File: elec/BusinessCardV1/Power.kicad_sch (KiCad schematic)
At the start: 0 parts

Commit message: Added BMA400
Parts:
- added U1: *, BMA400:XDCR_BMA400, symbol BMA400:BMA400
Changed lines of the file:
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@@
 	(generator_version "9.0")
 	(paper "A4")
+	(symbol
+		(lib_id "BMA400:BMA400")
+		(at 72.39 64.77 0)
+		(unit 1)
+		(exclude_from_sim no)
+		(in_bom yes)
+		(on_board yes)
+		(dnp no)
+		(fields_autoplaced yes)
+		(property "Reference" "U1"
+			(at 72.39 43.18 0)
+			(effects
+				(font
+					(size 1.8288 1.8288)
+				)
+			)
+		)
+		(property "Value" "*"
+			(at 72.39 46.99 0)
+			(effects
+				(font
+					(size 1.8288 1.8288)
+				)
+			)
+		)
+		(property "Footprint" "BMA400:XDCR_BMA400"
+			(at 72.39 64.77 0)
+			(effects
+				(font
+					(size 1.27 1.27)
+				)
+				(hide yes)
+			)
+		)
+		(property "Datasheet" ""
+			(at 72.39 64.77 0)
+			(effects
+				(font
+					(size 1.27 1.27)
+				)
+				(hide yes)
+			)
+		)
+		(property "Description" "Accelerometer X, Y, Z Axis ±2g, 4g, 8g, 16g - 12-LGA (2x2)"
+			(at 72.39 64.77 0)
+			(effects
+				(font
+					(size 1.27 1.27)
+				)
+				(hide yes)
+			)
+		)
+		(property "SnapEDA_Link" "https://www.snapeda.com/parts/BMA400/Bosch+Sensortec/view-part/?ref=snap"
+			(at 72.39 64.77 0)
+			(effects
+				(font
+					(size 1.8288 1.8288)
+				)
+				(justify left)
+				(hide yes)
+			)
+		)
+		(property "Package" "LGA-12 Bosch Tools"
+			(at 72.39 64.77 0)
+			(effects
+				(font
+					(size 1.8288 1.8288)
+				)
+				(justify left)
+				(hide yes)
+			)
+		)
+		(property "ALTIUM_VALUE" "*"
+			(at 72.39 64.77 0)
+			(effects
+				(font
+					(size 1.8288 1.8288)
+				)
+				(justify left)
+				(hide yes)
+			)
+		)
+		(property "MF" "Bosch Sensortec"
+			(at 72.39 64.77 0)
+			(effects
+				(font
+					(size 1.8288 1.8288)
+				)
+				(justify left)
+				(hide yes)
+			)
+		)
+		(property "MP" "BMA400"
+			(at 72.39 64.77 0)
+			(effects
+				(font
+					(size 1.8288 1.8288)
+				)
+				(justify left)
+				(hide yes)
+			)
+		)
+		(property "Check_prices" "https://www.snapeda.com/parts/BMA400/Bosch+Sensortec/view-part/?ref=eda"
+			(at 72.39 64.77 0)
+			(effects
+				(font
+					(size 1.8288 1.8288)
+				)
+				(justify left)
+				(hide yes)
+			)
+		)
+		(pin "7"
+		)
+		(pin "3"
+		)
+		(pin "10"
+		)
+		(pin "12"
+		)
+		(pin "2"
+		)
+		(pin "1"
+		)
+		(pin "5"
+		)
+		(pin "9"
+		)
+		(pin "6"
+		)
+		(pin "8"
+		)
+		(instances
+			(project ""
+				(path "/28a1e4b0-497b-455a-8c80-759850e7b173/9de3a60e-6635-4d18-85fa-31055f93e53d"
+					(reference "U1")
+					(unit 1)
+				)
+			)
+		)
+	)
 )

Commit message: Big Ballz
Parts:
- added D1: QBLP595-R, FP-QBLP595-R-MFG, symbol QBLP595:QTB-LED-0002

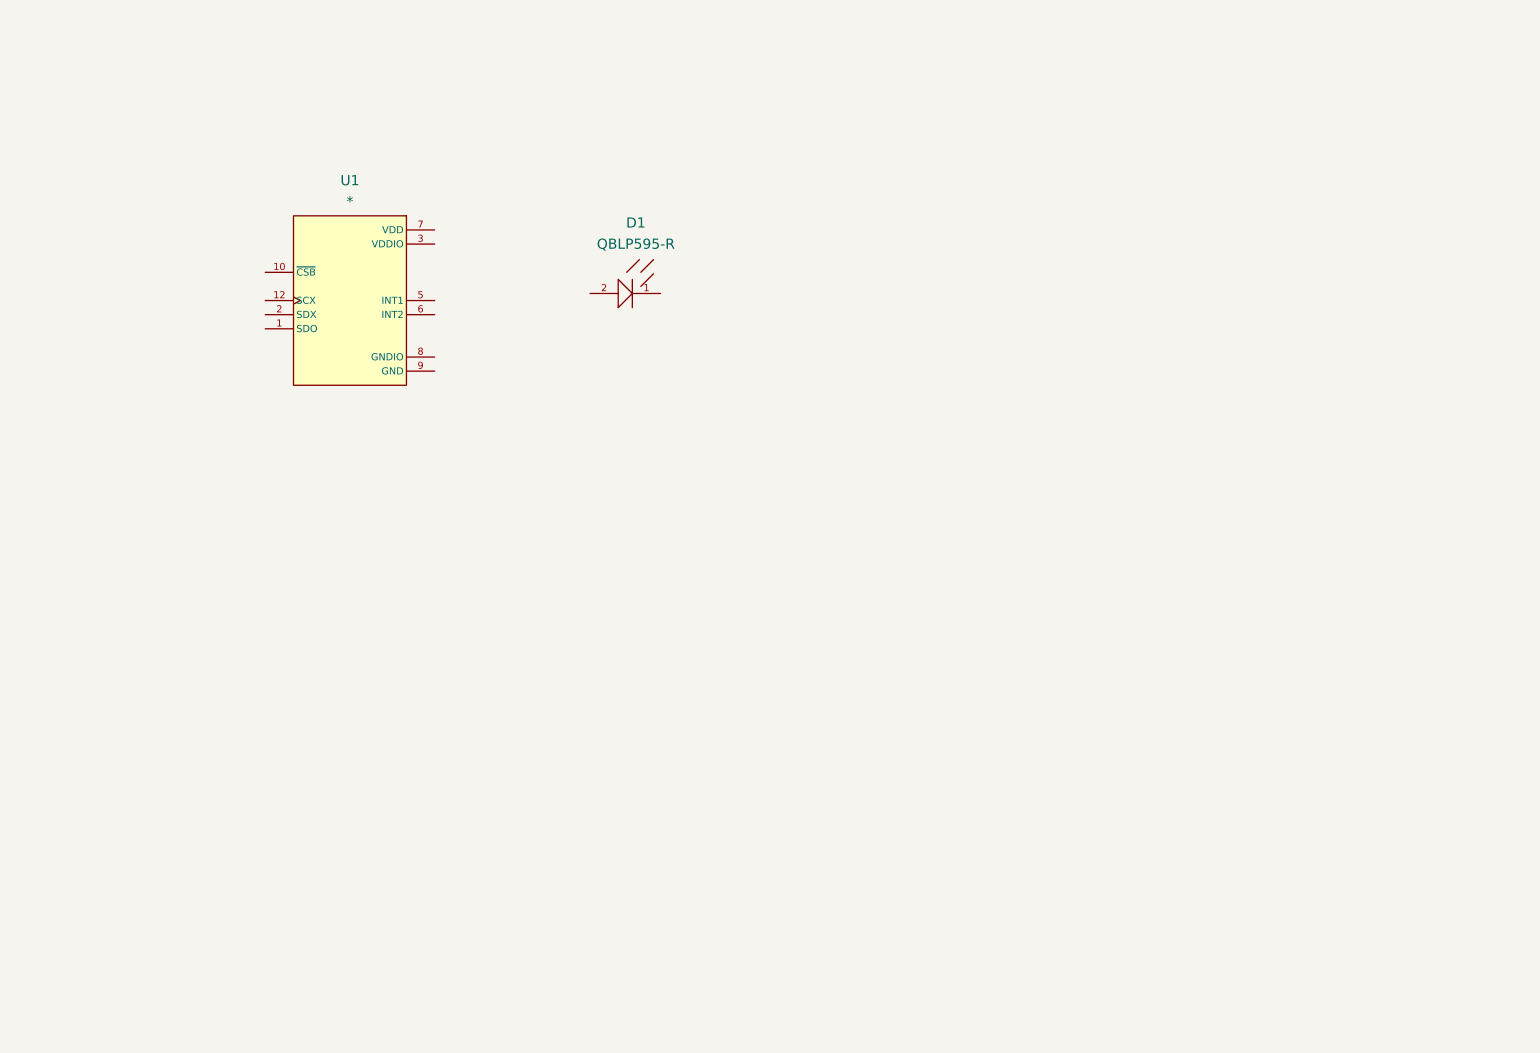
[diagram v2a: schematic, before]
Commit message: Started the power management
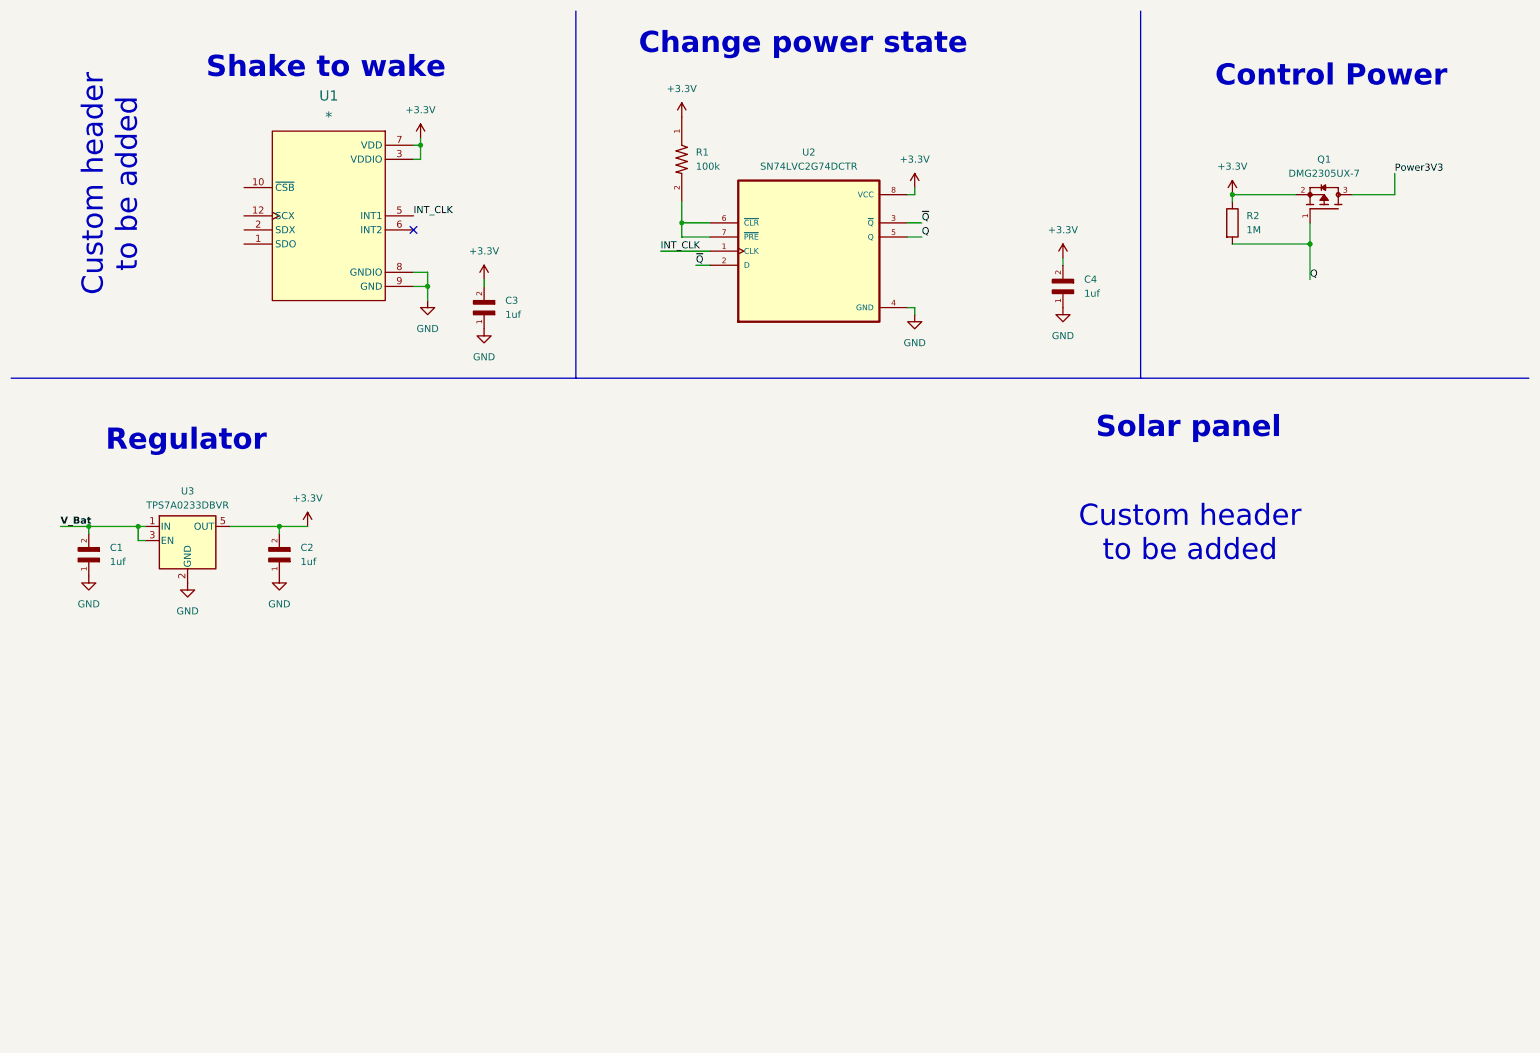
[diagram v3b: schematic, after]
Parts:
- removed D1: QBLP595-R, FP-QBLP595-R-MFG, symbol QBLP595:QTB-LED-0002
- added C1, C2, C3, C4: 1uf, CL10B105KP8NNNC:CAPC1608X90N, symbol CL10B105KP8NNNC:CL10B105KP8NNNC
- added Q1: DMG2305UX-7, DMG2305UX-7:SOT91P240X110-3N_DMG2305UX-7, symbol DMG2305UX-7:DMG2305UX-7
- added R1: 100k, RC0603FR-07100KL:RESC1607X60N, symbol RC0603FR-07100KL:RC0603FR-07100KL
- added R2: 1M, Resistor_SMD:R_0603_1608Metric_Pad0.98x0.95mm_HandSolder, symbol Device:R
- added U2: SN74LVC2G74DCTR, SN74LVC2G74DCTR:SOP65P400X130-8N, symbol SN74LVC2G74DCTR:SN74LVC2G74DCTR
- added U3: TPS7A0233DBVR, Package_TO_SOT_SMD:SOT-23-5, symbol Regulator_Linear:TLV70033_SOT23-5
- U1: DigiKey_Part_Number (none) -> BMA400
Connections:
- net +3.3V: now reaches U1.3 (VDDIO)
- net +3.3V: now also U1.7 (VDD), C2.2, C3.2, C4.2, Q1.2, R1.1, R2.1, U2.8 (VCC), U3.5 (OUT)
- net INT_CLK: now reaches U1.5 (INT1)
- net INT_CLK: now also U2.1 (CLK)
- net GND: now reaches U1.8 (GNDIO)
- net GND: now also U1.9 (GND), C1.1, C2.1, C3.1, C4.1, U2.4 (GND), U3.2 (GND)
- new net: R1.2, U2.6 (~{CLR}), U2.7 (~{PRE})
- new net Power3V3: Q1.3
- new net Q: Q1.1, R2.2, U2.5 (Q)
- new net V_Bat: C1.2, U3.1 (IN), U3.3 (EN)
- new net ~{Q}: U2.2 (D), U2.3 (~{Q})
- no-connect marks 0 -> 1
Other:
- note added: "Change power state"
- note added: "Control Power"
- note added: "Custom header to be added"
- note added: "Regulator"
- note added: "Shake to wake"
- note added: "Solar panel"
- moved on the sheet: U1

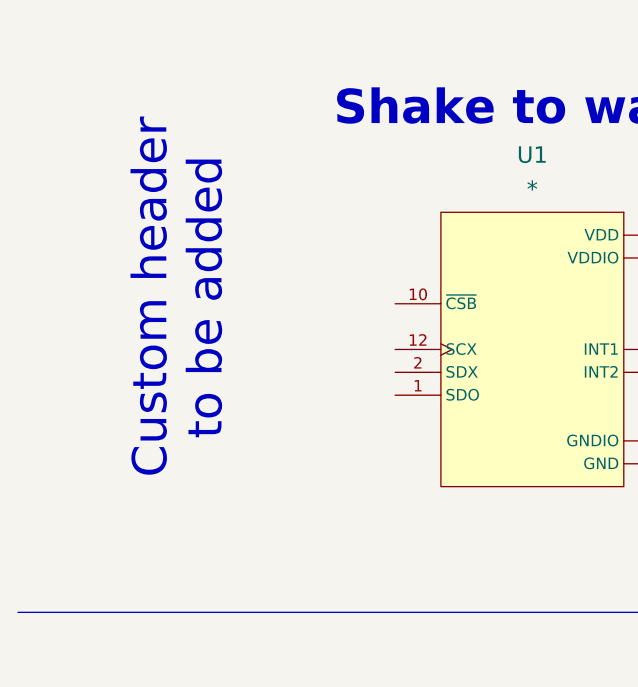
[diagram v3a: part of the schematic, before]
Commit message: Added header BMA400
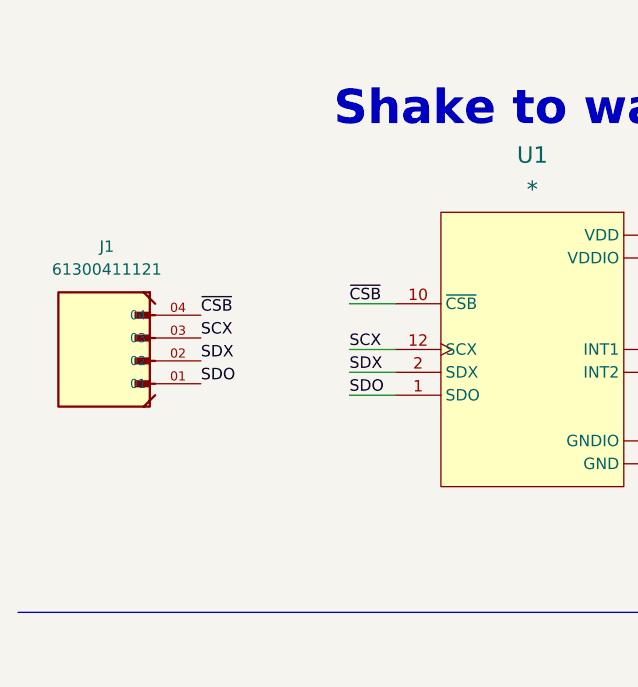
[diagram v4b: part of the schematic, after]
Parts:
- added J1: 61300411121, 61300411121:WURTH_61300411121, symbol Header1x4:61300411121
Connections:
- net SDO: now reaches U1.1 (SDO)
- net SDO: now also J1.01
- net ~{CSB}: now reaches U1.10 (~{CSB})
- net ~{CSB}: now also J1.04
- net SCX: now reaches U1.12 (SCX)
- net SCX: now also J1.03
- net SDX: now reaches U1.2 (SDX)
- net SDX: now also J1.02

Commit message: heheheha
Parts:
- added Q2: DMG2305UX-7, DMG2305UX-7:SOT91P240X110-3N_DMG2305UX-7, symbol DMG2305UX-7:DMG2305UX-7
- added R3: 1M, Resistor_SMD:R_0603_1608Metric_Pad0.98x0.95mm_HandSolder, symbol Device:R
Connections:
- net +3.3V: now also Q2.2, R3.1
- new net RingBTN: Q2.1, R3.2
- new net RingPower: Q2.3
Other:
- note added: "Ring Power"

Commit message: Power finished
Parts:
- added C5, C6: 4u7, CL10A475KP8NNNC:CAPC1608X90N, symbol CL10A475KP8NNNC:CL10A475KP8NNNC
- added J2: 6130XX11121_61300211121, 6130XX11121_61300211121:61300211121, symbol Header1x2:6130XX11121_61300211121
- added R5: 69K8, RC0603FR-0769K8L:RESC1608X55N, symbol RC0603FR-0769K8L:RC0603FR-0769K8L
- added U14: MCP73831T-2DCI_OT, MCP73831T-2DCI_OT:SOT95P270X145-5N, symbol MCP73831T-2DCI_OT:MCP73831T-2DCI_OT
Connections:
- net GND: now also C5.1, C6.1, J2.1, U14.2 (VSS)
- net V_Bat: now also C6.2, U14.3 (VBAT)
- new net: R5.1, U14.5 (PROG)
- new net SolarPower: C5.2, J2.2, R5.2, U14.4 (VDD)
- no-connect marks 1 -> 2
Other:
- note added: "Charger"
- note removed: "Custom header to be added"
- moved on the sheet: C1, C2, U3

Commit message: All footprint and start of PCB
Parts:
- J1: footprint 61300411121:WURTH_61300411121 -> HEADER1x4:HEADER1x4_SMD
- J2: footprint 6130XX11121_61300211121:61300211121 -> Header1x2:Header1x2_SMD
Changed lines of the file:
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@@
 			)
 		)
-		(property "Footprint" "6130XX11121_61300211121:61300211121"
+		(property "Footprint" "Header1x2:Header1x2_SMD"
 			(at 242.57 100.33 0)
 			(effects
@@
 			)
 		)
-		(property "Footprint" "61300411121:WURTH_61300411121"
+		(property "Footprint" "HEADER1x4:HEADER1x4_SMD"
 			(at 21.59 48.26 0)
 			(effects
